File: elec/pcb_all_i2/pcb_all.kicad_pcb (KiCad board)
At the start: 2 copper layers, 59.2 x 116.5 mm, 84 parts, among them IC1 TPS629203QDRLRQ1, IC2 AP63203WU-7, IC3 BQ25176MDSGR, IC4 TPS61023DRLR, IC5 BMP390, IC6 LSM6DSLTR, J1 Conn_01x02, J2 Conn_01x07, Q1 CSD16301Q2, Q2 CSD16301Q2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

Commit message: did stuff
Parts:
- removed C15: 22uF, Capacitor_SMD:C_1206_3216Metric
- removed D8: SS14-M3_5AT, footprints:DIOM5127X229N
- removed IC1: TPS629203QDRLRQ1, footprints:SOTFL50P160X60-8N
- removed IC4: TPS61023DRLR, footprints:SOTFL50P160X60-6N
- removed L3: 1uH, Inductor_SMD:L_1008_2520Metric
- removed R15: 68k, Resistor_SMD:R_0603_1608Metric
- removed R16: 510k, Resistor_SMD:R_0603_1608Metric
- removed R24, R25: 2k, Resistor_SMD:R_0603_1608Metric
- removed R26: 30k, Resistor_SMD:R_0603_1608Metric
- removed R27: 4.7k, Resistor_SMD:R_0603_1608Metric
- removed TP3: TestPoint_2Pole, Connector_PinHeader_2.54mm:PinHeader_1x02_P2.54mm_Vertical
- added H1: MountingHole, MountingHole:MountingHole_2.2mm_M2_DIN965_Pad, F.Cu at (144.8, 83.8)
- added H2: MountingHole, MountingHole:MountingHole_2.2mm_M2_DIN965_Pad, F.Cu at (190.3, 83.8)
- added H3: MountingHole, MountingHole:MountingHole_2.2mm_M2_DIN965_Pad, F.Cu at (144.8, 117.8)
- added H4: MountingHole, MountingHole:MountingHole_2.2mm_M2_DIN965_Pad, F.Cu at (190.3, 117.8)
- added PS1: TPS61022RWUR, footprints:TPS61022RWUR, F.Cu at (46.0, 79.6)
- added SW1: SW_DPST_x2, footprints:push_button, F.Cu at (177.4, 88.6)
- added SW2: SW_DPST_x2, footprints:psuh_button_side, F.Cu at (167.6, 82.8)
- added SW3: SW_DPST_x2, footprints:psuh_button_side, F.Cu at (167.6, 118.8)
- BT1: footprint Connector_JST:JST_XH_B2B-XH-A_1x02_P2.50mm_Vertical -> Connector_JST:JST_SH_BM02B-SRSS-TB_1x02-1MP_P1.00mm_Vertical
- C1: value 4.7uF -> 10uF
- C11: value 10uF -> 22uF
- J1: footprint Connector_JST:JST_XH_B2B-XH-A_1x02_P2.50mm_Vertical -> Connector_PinHeader_1.00mm:PinHeader_1x02_P1.00mm_Vertical
- J2: moved to B.Cu
- L1: value 2.2uH -> 1uH
- L2: value 4.7uH -> 3.9uH
- R1: value 30k -> 732k
- R5: value 30k -> 100k
- moved C13 92.9 mm to (40.4, 81.6), turned to 0 degrees
- moved C1 90.4 mm to (40.4, 71.6), turned to 0 degrees
- moved C3 87.0 mm to (40.4, 74.9), turned to 0 degrees
- moved C11 83.8 mm to (40.4, 78.3)
- moved TP8 79.8 mm to (45.6, 72.2), turned to 0 degrees
- moved R1 76.5 mm to (50.8, 78.3), turned to 0 degrees
- moved L1 75.4 mm to (50.3, 71.8), turned to 0 degrees
- moved R5 71.7 mm to (50.8, 80.8), turned to 0 degrees
- moved B1 66.7 mm to (187.0, 110.5), turned to 90 degrees
- moved C10 62.7 mm to (86.8, 79.5)
- moved C12 62.7 mm to (97.4, 76.9)
- moved C14 62.7 mm to (100.1, 109.9)
- moved C19 62.7 mm to (81.8, 106.2)
- moved C21 62.7 mm to (66.8, 103.4)
- moved C22 62.7 mm to (85.0, 103.0)
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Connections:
- net Net-(BT1--) renamed /vss
- net Net-(U1-V-) renamed /v-
- C11 pad 1: +BATT -> +5V
- C3 pad 1: +1V8 -> +5V
- L1 pad 1: Net-(IC1-SW) -> +BATT
- L1 pad 2: +1V8 -> Net-(PS1-SW)
- R1 pad 1: Net-(IC1-MODE/S-CONF) -> +5V
- R1 pad 2: Net-(R1-Pad2) -> Net-(PS1-FB)
- R5 pad 1: Net-(IC1-FB/VSET) -> Net-(PS1-FB)
- R5 pad 2: Net-(R26-Pad2) -> GND
- U2 pad 1: /A (MIC) -> /BUTTON-A
- U2 pad 11: unconnected-(U2-D10-Pad11) -> /BUTTON-B
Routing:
- net +BATT: track 100.1 -> 32.8 mm, vias 20 -> 0
- net +5V: track 160.3 -> 93.3 mm
- net /TX (SIM7600G-H): track 46.0 -> 20.2 mm
- net +3V3: track 116.3 -> 94.3 mm, vias 7 -> 5
- net /PWM (Vibration): track 33.3 -> 14.2 mm, vias 2 -> 1
- net /BATT VOLTAGE: track 68.9 -> 51.4 mm, vias 3 -> 2
- net /INT1 (IMU): track 46.7 -> 33.4 mm
- net /SDA: track 67.8 -> 56.1 mm
- net /SCL: track 70.0 -> 60.5 mm
- net /vss: track 37.6 -> 28.5 mm
- net /SLEEP (SIM7600G-H): track 23.2 -> 18.7 mm
- net /RX (SIM7600G-H): track 58.0 -> 54.3 mm
- net Net-(IC1-FB/VSET): track 3.12 -> 0.00 mm
- net Net-(IC4-FB): track 2.90 -> 0.00 mm
- net Net-(IC1-SW): track 1.77 -> 0.00 mm
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- removed copper zone on F.Cu, net (none)
- removed copper zone on B.Cu, net +BATT
- removed copper zone on F.Cu, net Net-(D8-A)
- removed copper zone on F.Cu, net Net-(IC4-SW)
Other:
- board size 59.2 x 116.5 mm -> 50.5 x 39.5 mm
- board text removed: "1v8 Buck"
- board text removed: "3v3 Buck"
- board text removed: "5v Boost"
- board text removed: "Barometer Module"
- board text removed: "Battery"
- board text removed: "Battery Protection"
- board text removed: "Charging IC"
- board text removed: "Chen-Xuan"
- board text removed: "IMU Module"
- board text removed: "LTE & GNSS Module"
- board text removed: "Microcontroller"
- board text removed: "Vibration Module"
- board text removed: "Wireless Charging"
- board text removed: "designed by the tripcharmers"
- board text removed: "revision 1 28/4/25 JLCJLCJLCJLC"

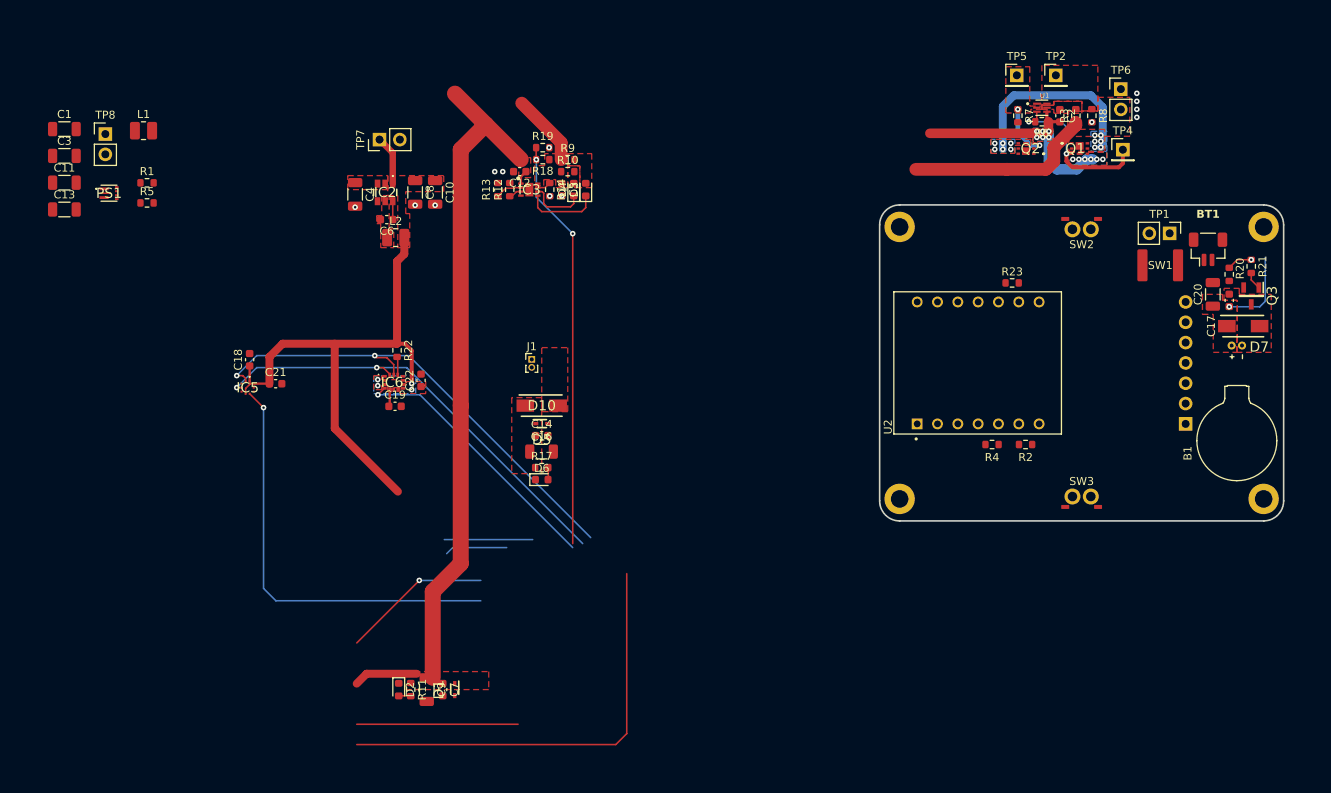
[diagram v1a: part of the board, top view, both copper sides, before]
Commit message: allllmost done; just need to trace modules together
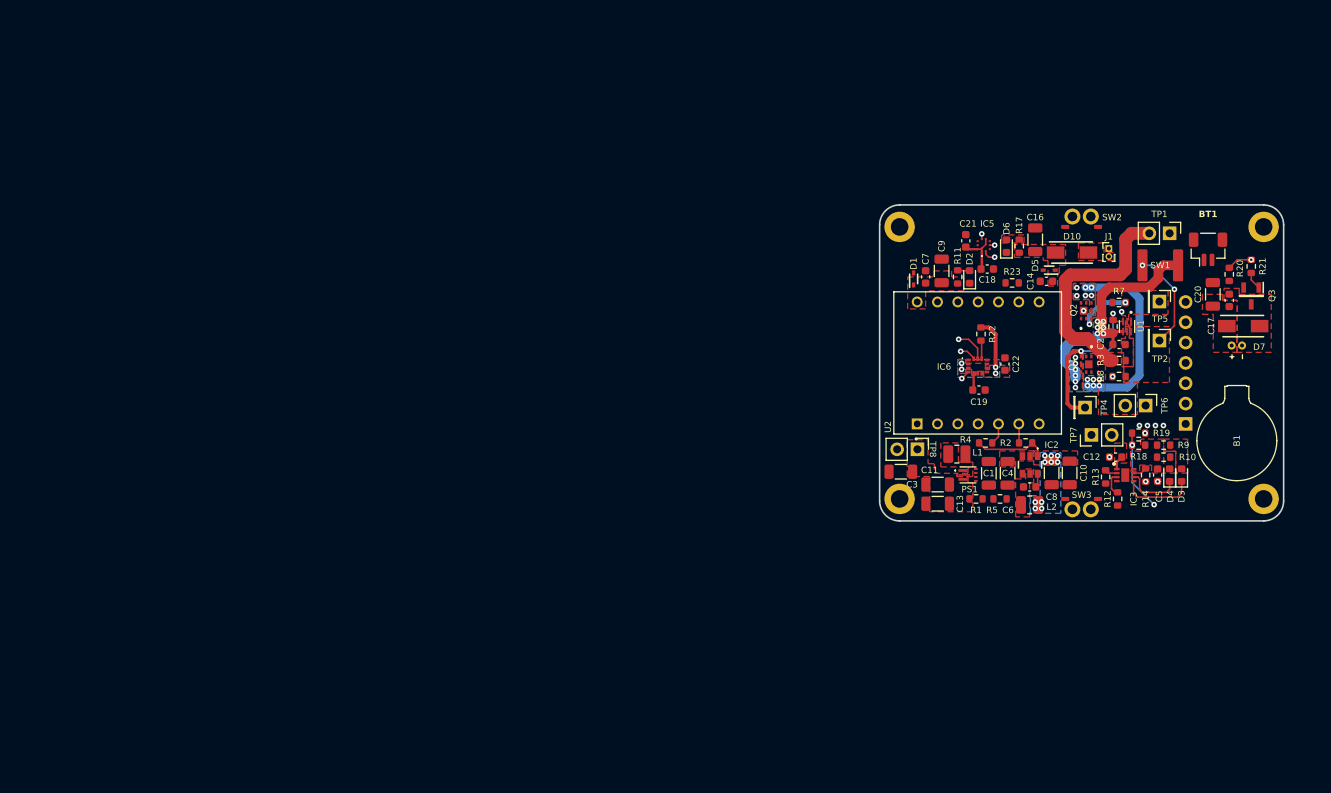
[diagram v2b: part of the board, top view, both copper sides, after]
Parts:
- moved C1 123.3 mm to (156.0, 114.6), turned to 90 degrees
- moved C11 115.5 mm to (149.6, 116.0), turned to 180 degrees
- moved C13 115.2 mm to (149.6, 118.4), turned to 180 degrees
- moved PS1 113.0 mm to (153.4, 114.8)
- moved R5 112.9 mm to (157.4, 117.8)
- moved C3 111.8 mm to (145.0, 114.4), turned to 180 degrees
- moved R1 110.9 mm to (154.4, 117.8)
- moved L1 109.4 mm to (152.0, 112.2), turned to 180 degrees
- moved TP8 108.9 mm to (147.1, 111.6), turned to -90 degrees
- moved TP7 96.3 mm to (168.8, 109.8)
- moved IC5 93.7 mm to (155.4, 86.1), turned to 180 degrees
- moved C18 92.9 mm to (155.8, 89.1), turned to 0 degrees
- moved C4 88.7 mm to (158.3, 114.6)
- moved C21 88.1 mm to (153.1, 85.5), turned to 90 degrees
- moved D2 88.1 mm to (153.6, 90.0), turned to 90 degrees
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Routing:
- net +5V: track 93.3 -> 1.76 mm
- net +3V3: track 94.3 -> 24.1 mm, vias 5 -> 14
- net /RX (SIM7600G-H): track 54.3 -> 0.00 mm
- net /INT (BAROMETER): track 52.8 -> 0.65 mm
- net /SCL: track 60.5 -> 8.32 mm
- net /SDA: track 56.1 -> 5.38 mm
- net /BATT VOLTAGE: track 51.4 -> 10.1 mm
- net /INT1 (IMU): track 33.4 -> 1.15 mm
- net /TX (SIM7600G-H): track 20.2 -> 0.00 mm
- net /SLEEP (SIM7600G-H): track 18.7 -> 0.00 mm, vias 1 -> 0
- net /v-: track 0.00 -> 12.4 mm, vias 0 -> 2
- net /PWM (Vibration): track 14.2 -> 3.16 mm
- net +BATT: track 32.8 -> 28.8 mm
- net Net-(IC3-ISET): track 3.35 -> 1.54 mm
- net Net-(D6-A): track 1.52 -> 0.00 mm
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- added copper zone on F.Cu, net Net-(D6-A)
- added copper zone on F.Cu, net Net-(PS1-SW)

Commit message: some traces (3v3 and 5v)
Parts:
- moved R22 0.21 mm to (155.0, 97.4)
- turned C12 to 0 degrees
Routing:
- net +3V3: track 24.1 -> 65.7 mm, vias 14 -> 16
- net +5V: track 1.76 -> 27.4 mm, vias 0 -> 9
- net +BATT: track 28.8 -> 48.4 mm
- net Net-(PS1-FB): track 0.00 -> 3.95 mm
- net /SLEEP (SIM7600G-H): track 0.00 -> 2.38 mm
- net GND: vias 11 -> 12
- added copper zone on B.Cu, net +5V

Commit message: all done excpet pcba
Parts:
- added R15: 4.7k, Resistor_SMD:R_0603_1608Metric, F.Cu at (153.8, 95.0)
- added R16: 4.7k, Resistor_SMD:R_0603_1608Metric, F.Cu at (146.6, 105.4)
- moved R19 27.0 mm to (148.1, 105.4), turned to 90 degrees
- moved R18 25.8 mm to (149.6, 105.4), turned to -90 degrees
- moved BT1 0.40 mm to (183.4, 86.2)
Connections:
- U2 pad 1: /BUTTON-A -> /BUTTON-B
- U2 pad 11: /BUTTON-B -> /BUTTON-A
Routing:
- net /PWM (Vibration): track 3.16 -> 80.0 mm
- net +5V: track 27.4 -> 82.9 mm, vias 9 -> 25
- net /SCL: track 8.32 -> 61.2 mm
- net +3V3: track 65.7 -> 116.2 mm, vias 16 -> 28
- net /SLEEP (SIM7600G-H): track 2.38 -> 48.8 mm
- net /SDA: track 5.38 -> 51.1 mm, vias 2 -> 1
- net /RX (SIM7600G-H): track 0.00 -> 40.2 mm, vias 0 -> 3
- net /TX (SIM7600G-H): track 0.00 -> 30.4 mm
- net /BUTTON-B: track 0.00 -> 29.0 mm, vias 0 -> 1
- net /BUTTON-A: track 0.00 -> 24.5 mm, vias 0 -> 1
- net +BATT: track 48.4 -> 70.1 mm
- net /INT (BAROMETER): track 0.65 -> 10.0 mm
- net /BATT VOLTAGE: track 10.1 -> 3.68 mm, vias 2 -> 0
- net /INT1 (IMU): track 1.15 -> 7.03 mm, vias 1 -> 0
- net /vss: track 29.8 -> 34.2 mm
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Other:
- board text added: "#include <love.h>"
- board text added: "Kid you not they're Safe"
- board text added: "NCX"
- board text added: "NCX, TWX WYJ, HMZ"
- board text added: "Product of tripcharm."
- board text added: "Who needs script when you've got (trip)charm."
- board text added: "if (lost) return home"
- board text added: "orginated in Singapore; designed in Singapore; assembled in Singapore"
- board text added: "tripcharm. revision 2 20/7/25 | JLC Order No. JLCJLCJLCJLC designed by the tripcharmers signed, Ng Chen-Xuan"
- board text added: "while (safe) { smile++; }"

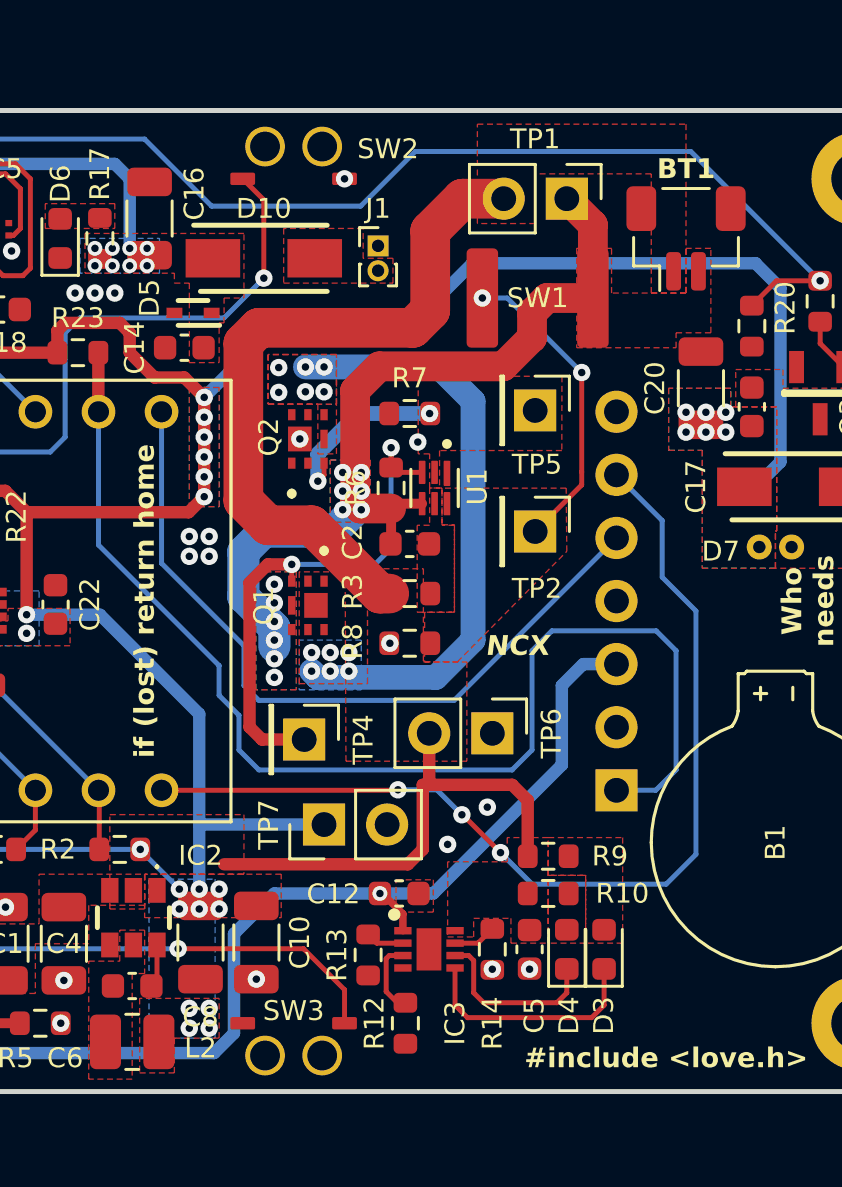
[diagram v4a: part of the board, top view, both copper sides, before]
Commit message: made dfm happy
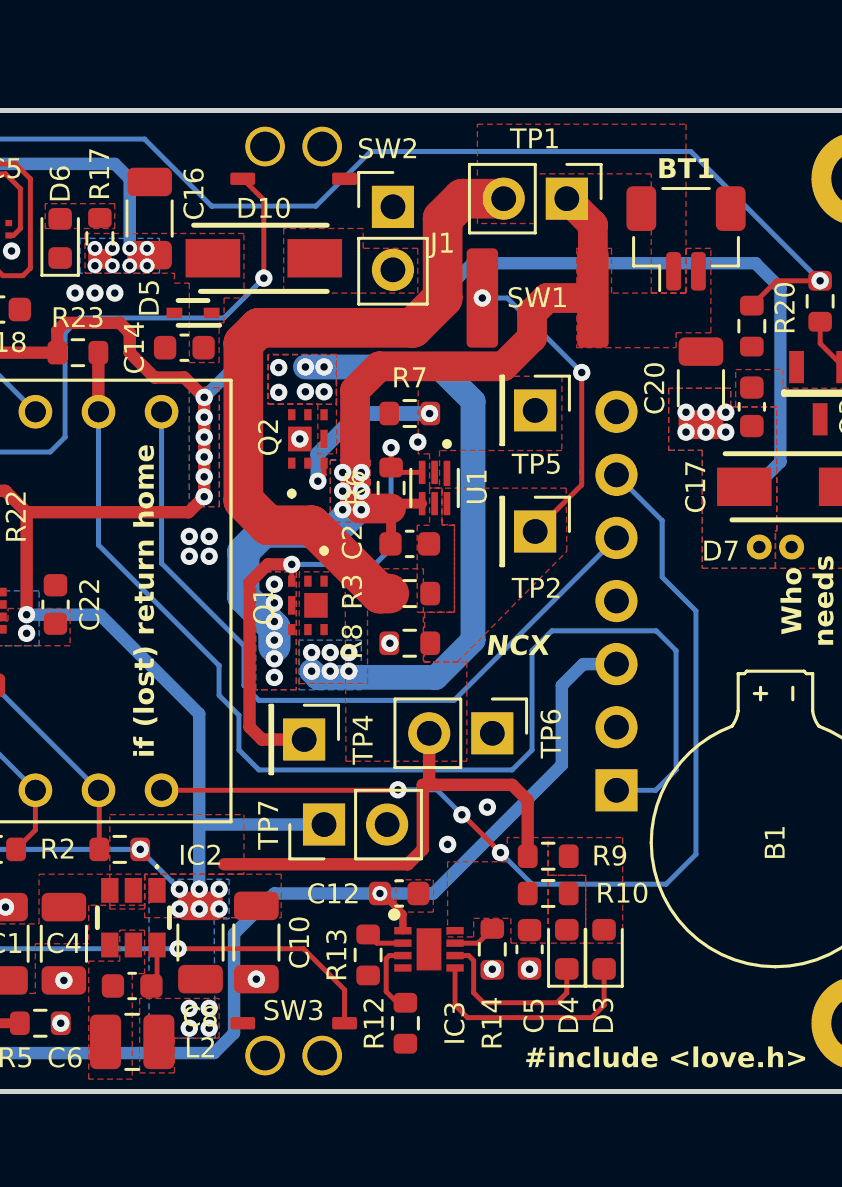
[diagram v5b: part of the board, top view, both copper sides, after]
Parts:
- J1: footprint Connector_PinHeader_1.00mm:PinHeader_1x02_P1.00mm_Vertical -> Connector_PinHeader_2.54mm:PinHeader_1x02_P2.54mm_Vertical
- moved J1 1.69 mm to (171.6, 84.9)
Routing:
- net GND: vias 22 -> 21

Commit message: completed elec?
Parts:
- R3: value R330 -> 330R
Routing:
- net /SLEEP (SIM7600G-H): track 48.8 -> 40.7 mm, vias 0 -> 1
- net /TX (SIM7600G-H): track 30.4 -> 31.6 mm
- net /SDA: track 51.1 -> 50.3 mm
- net Net-(Q1-G): track 21.4 -> 22.2 mm
